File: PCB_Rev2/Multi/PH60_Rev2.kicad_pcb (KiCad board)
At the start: 2 copper layers, 285 x 94.6 mm, 182 parts, among them J1 USB_C_Receptacle_USB2.0_16P, J2 Conn_01x02, U2 W25Q128JVS, U3 RP2040, U4 XC6206PxxxMR, Y1 Crystal_GND24

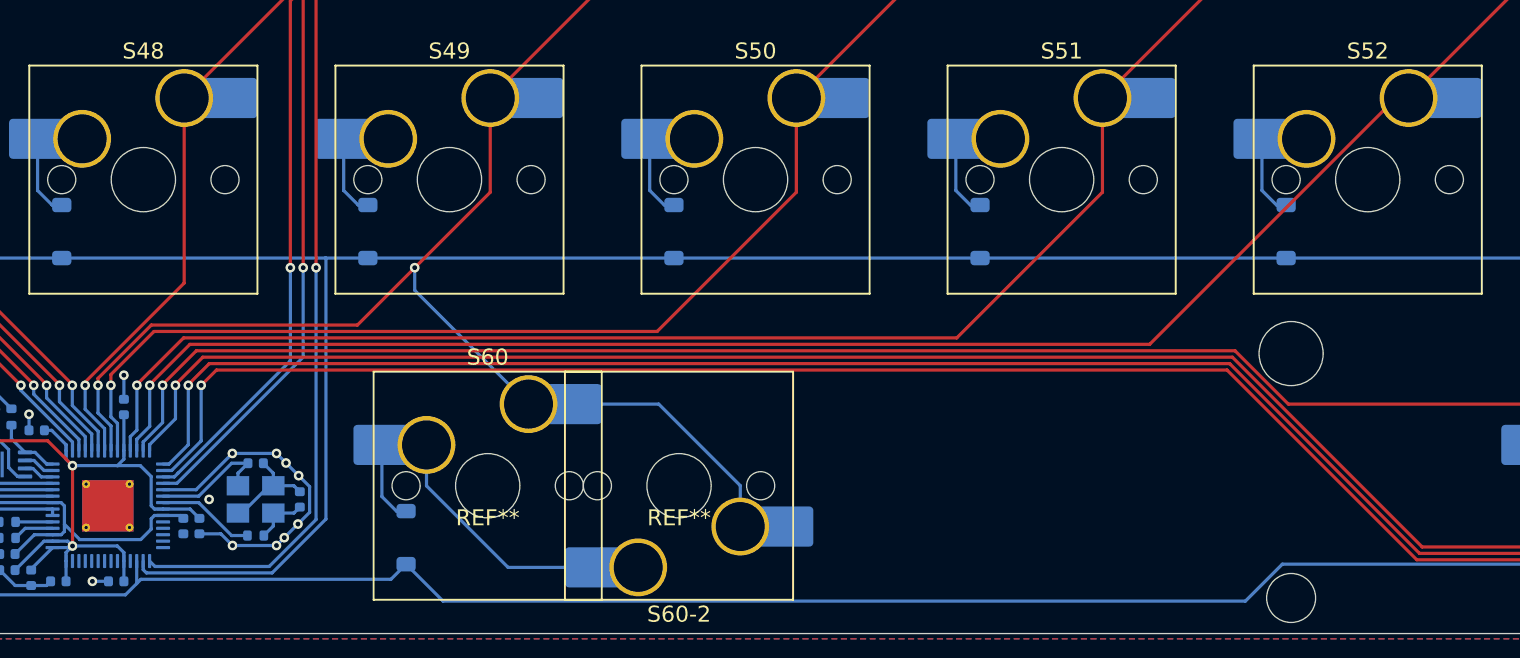
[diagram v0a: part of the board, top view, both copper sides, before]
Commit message: Delete Stacked Silkscreen
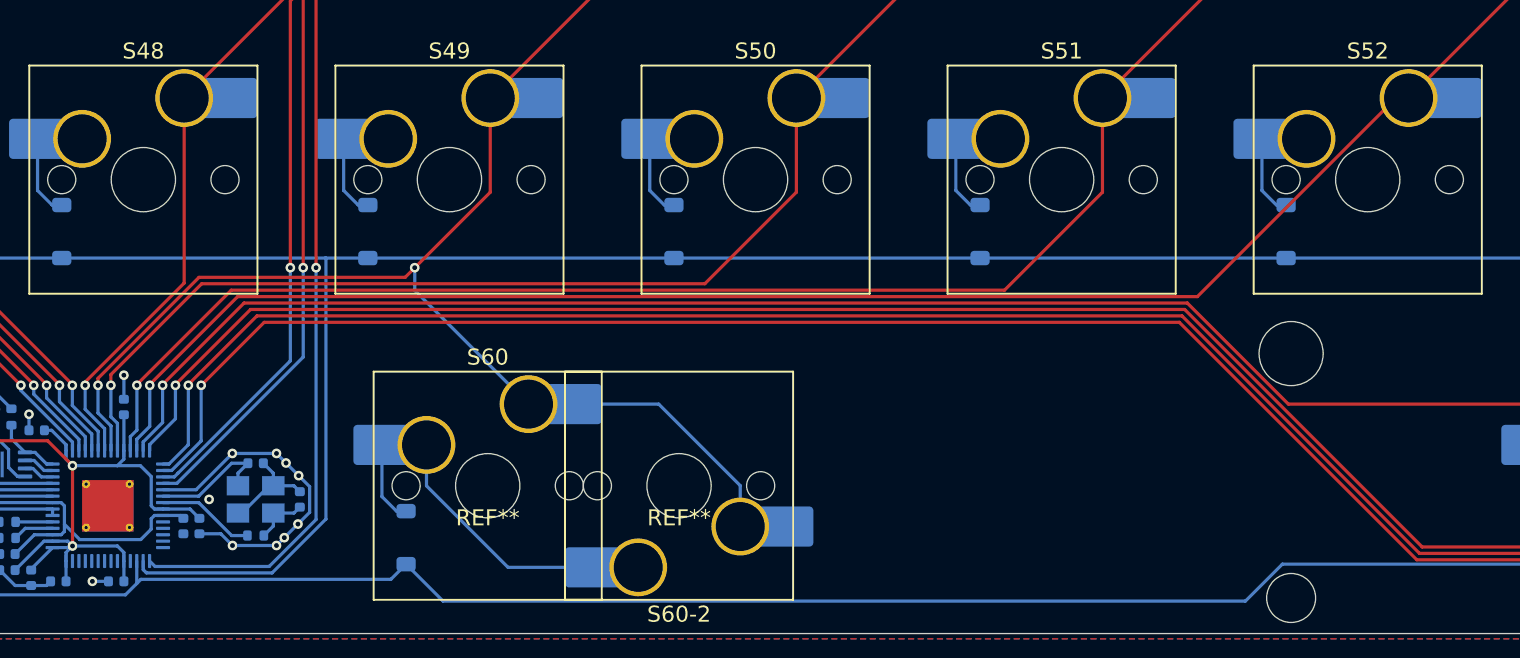
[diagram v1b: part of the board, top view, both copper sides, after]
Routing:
- net col_13: track 325.9 -> 328.4 mm
- net col_10: track 188.1 -> 190.6 mm
- net col_11: track 226.4 -> 228.8 mm
- net col_12: track 311.2 -> 313.7 mm

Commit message: Update PH60_Rev2.kicad_pcb
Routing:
- net col_9: track 157.2 -> 160.6 mm
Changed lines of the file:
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@@
 	)
 	(segment
-		(start 203.709098 102.53)
-		(end 143.981471 102.53)
+		(start 138.51 108.001471)
+		(end 138.51 108.05)
+		(width 0.2)
+		(layer "F.Cu")
+		(net 96)
+	)
+	(segment
+		(start 216.8525 90.17)
+		(end 216.8525 96.033402)
 		(width 0.2)
 		(layer "F.Cu")
@@
 	)
 	(segment
-		(start 143.981471 102.53)
-		(end 138.51 108.001471)
-		(width 0.2)
-		(layer "F.Cu")
-		(net 96)
-	)
-	(segment
 		(start 221.615 52.07)
 		(end 221.615 42.545)
@@
 	)
 	(segment
-		(start 216.8525 90.17)
-		(end 216.069098 90.17)
+		(start 143.981471 102.53)
+		(end 138.51 108.001471)
 		(width 0.2)
 		(layer "F.Cu")
@@
 	)
 	(segment
-		(start 216.069098 90.17)
-		(end 203.709098 102.53)
+		(start 210.355902 102.53)
+		(end 143.981471 102.53)
 		(width 0.2)
 		(layer "F.Cu")
@@
 	)
 	(segment
-		(start 138.51 108.001471)
-		(end 138.51 108.05)
+		(start 216.8525 96.033402)
+		(end 210.355902 102.53)
 		(width 0.2)
 		(layer "F.Cu")

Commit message: Ground Plane Continuity Improvement
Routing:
- net GND: track 49.6 -> 65.2 mm, vias 15 -> 21
- removed copper zone on B.Cu, net GND

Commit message: PCB Wiring Enhancement
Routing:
- net col_13: track 328.4 -> 329.5 mm
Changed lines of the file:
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@@
 		)
 		(pad "" np_thru_hole circle
+			(at 2.54 -5.08 180)
+			(size 3.05 3.05)
+			(drill 3.05)
+			(layers "F&B.Cu" "*.Mask")
+			(pinfunction "2")
+			(pintype "passive")
+		)
+		(pad "" np_thru_hole circle
 			(at 5.08 0 180)
 			(size 1.75 1.75)
@@
 			(pintype "passive")
 		)
-		(pad "2" thru_hole circle
-			(at 2.54 -5.08 180)
-			(size 3.6 3.6)
-			(drill 3.05)
-			(layers "*.Cu" "*.Mask")
-			(remove_unused_layers no)
-			(net 100 "col_13")
-			(pinfunction "2")
-			(pintype "passive")
-		)
 		(pad "2" smd roundrect
 			(at 5.32 -5.08 180)
@@
 	)
 	(segment
-		(start 283.21 37.316598)
-		(end 287.506598 33.02)
-		(width 0.2)
-		(layer "B.Cu")
-		(net 100)
-	)
-	(segment
 		(start 302.26 43.18)
 		(end 302.26 34.685)
@@
 	)
 	(segment
-		(start 287.506598 33.02)
-		(end 297.815 33.02)
-		(width 0.2)
-		(layer "B.Cu")
-		(net 100)
-	)
-	(segment
 		(start 306.23375 120.885)
 		(end 307.49875 119.62)
@@
 	)
 	(segment
+		(start 287.506598 33.02)
+		(end 297.815 33.02)
+		(width 0.2)
+		(layer "B.Cu")
+		(net 100)
+	)
+	(segment
+		(start 280.43 40.096598)
+		(end 287.506598 33.02)
+		(width 0.2)
+		(layer "B.Cu")
+		(net 100)
+	)
+	(segment
 		(start 139.87136 113.35)
 		(end 141.71 111.51136)
@@
 	)
 	(segment
-		(start 283.21 43.18)
-		(end 283.21 37.316598)
+		(start 280.43 43.18)
+		(end 280.43 40.096598)
 		(width 0.2)
 		(layer "B.Cu")
